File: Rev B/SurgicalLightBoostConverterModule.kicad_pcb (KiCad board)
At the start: 2 copper layers, 140 x 90 mm, 96 parts, among them J1 2x7 P2.54mm, Q1 BC337, Q10 BC327, Q2 BC337, Q3 BC337, Q4 AOT240L, Q5 AOT240L, Q6 AOT240L, Q7 BC327, Q8 BC327, Q9 BC327, U1 TL494, U2 TL431D, U3 LM358

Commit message: Silk screen.
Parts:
- moved J1 26.0 mm to (90.0, 103.7)
- moved TP11 12.2 mm to (90.0, 98.0)
- moved TP8 7.36 mm to (85.0, 98.0)
- moved TP9 7.32 mm to (79.5, 98.0)
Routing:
- net /1IN+: track 45.7 -> 37.0 mm
- net /DTC: track 33.6 -> 25.5 mm
- net /2IN+: track 42.8 -> 35.3 mm, vias 0 -> 1
- net Net-(JP6-A): track 39.0 -> 31.5 mm
- net Net-(JP2-A): track 47.0 -> 40.1 mm
- net /1IN-: track 40.8 -> 34.1 mm
- net Net-(JP3-A): track 35.5 -> 29.4 mm
- net /FB: track 37.3 -> 32.4 mm
- net /2IN-: track 36.1 -> 32.7 mm
- net +5V: track 66.1 -> 67.7 mm
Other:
- board text added: "24V 10A Fuse"

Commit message: Updated text for testpoints and jumpers.
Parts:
- renumbered TP9 to 1IN+, TP8 to 1IN-, TP11 to DTC
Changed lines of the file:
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@@
 		(descr "wire loop with bead as test point, loop diameter2.548mm, hole diameter 1.5mm")
 		(tags "test point wire loop bead")
-		(property "Reference" "TP8"
-			(at 0.7 2.5 0)
+		(property "Reference" "1IN-"
+			(at 0 3 0)
 			(layer "F.SilkS")
 			(effects
@@
 		)
 		(fp_text user "${REFERENCE}"
-			(at 0.7 2.5 0)
+			(at 0 3 0)
 			(layer "F.Fab")
 			(effects
@@
 		(descr "wire loop with bead as test point, loop diameter2.548mm, hole diameter 1.5mm")
 		(tags "test point wire loop bead")
-		(property "Reference" "TP9"
-			(at 0.7 2.5 0)
+		(property "Reference" "1IN+"
+			(at 0 3 0)
 			(layer "F.SilkS")
 			(effects
@@
 		)
 		(fp_text user "${REFERENCE}"
-			(at 0.7 2.5 0)
+			(at 0 3 0)
 			(layer "F.Fab")
 			(effects
@@
 		(descr "wire loop with bead as test point, loop diameter2.548mm, hole diameter 1.5mm")
 		(tags "test point wire loop bead")
-		(property "Reference" "TP11"
-			(at 0.7 2.5 0)
+		(property "Reference" "DTC"
+			(at 0 3 0)
 			(layer "F.SilkS")
 			(effects
@@
 		)
 		(fp_text user "${REFERENCE}"
-			(at 0.7 2.5 0)
-			(layer "F.Fab")
-			(effects
+			(at 0 3 0)
+			(layer "F.Fab")
+			(effects

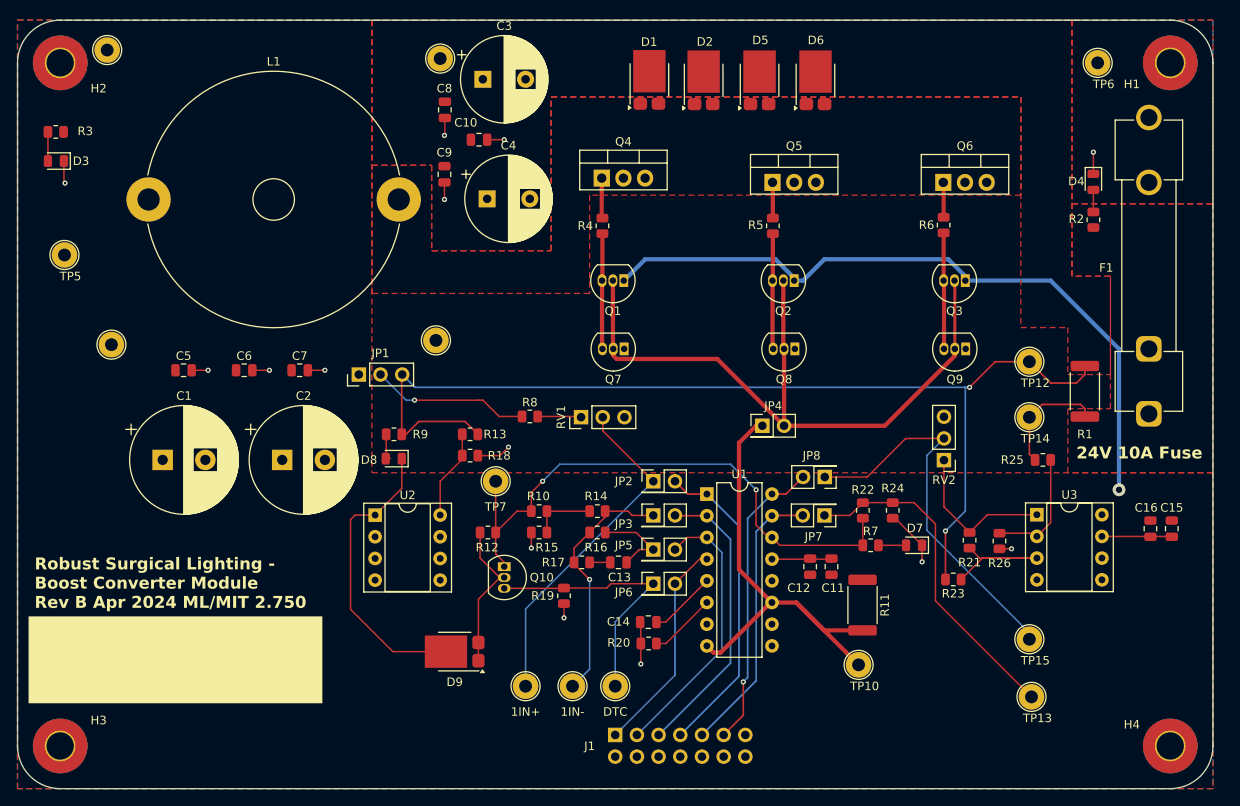
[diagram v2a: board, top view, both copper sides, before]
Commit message: Updated text for testpoints and jumpers.
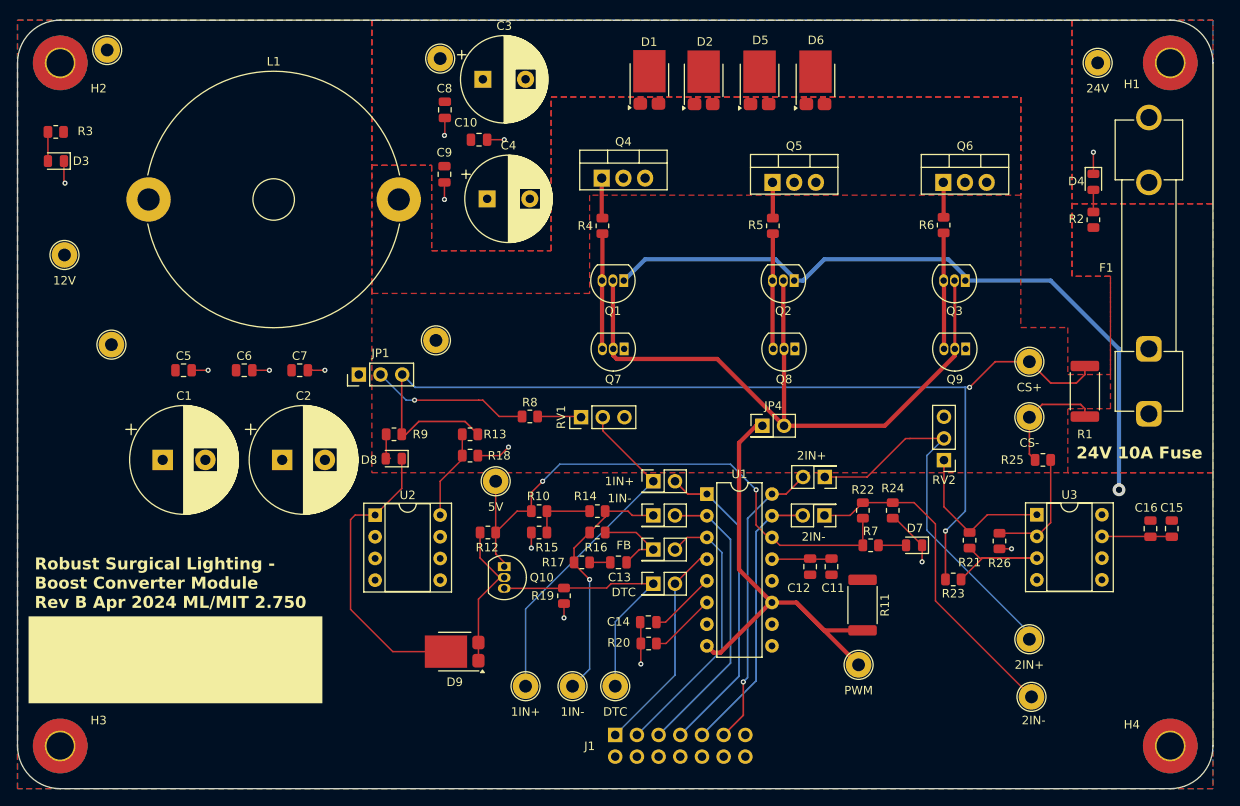
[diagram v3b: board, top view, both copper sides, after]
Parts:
- renumbered TP5 to 12V, JP2 to 1IN+, JP3 to 1IN-, TP6 to 24V, JP8 to 2IN+, TP15 to 2IN+, TP13 to 2IN-, JP7 to 2IN-, TP7 to 5V, TP12 to CS+, TP14 to CS-, JP6 to DTC, JP5 to FB, TP10 to PWM
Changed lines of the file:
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@@
 		(descr "wire loop with bead as test point, loop diameter2.548mm, hole diameter 1.5mm")
 		(tags "test point wire loop bead")
-		(property "Reference" "TP7"
+		(property "Reference" "5V"
 			(at 0 3 0)
 			(layer "F.SilkS")
@@
 		)
 		(fp_text user "${REFERENCE}"
-			(at 0.7 2.5 0)
+			(at 0 3 0)
 			(layer "F.Fab")
 			(effects
@@
 		(descr "wire loop with bead as test point, loop diameter2.548mm, hole diameter 1.5mm")
 		(tags "test point wire loop bead")
-		(property "Reference" "TP14"
-			(at 0.7 2.5 0)
+		(property "Reference" "CS-"
+			(at 0 3 0)
 			(layer "F.SilkS")
 			(effects
@@
 		)
 		(fp_text user "${REFERENCE}"
-			(at 0.7 2.5 0)
+			(at 0 3 0)
 			(layer "F.Fab")
 			(effects
@@
 		(descr "wire loop with bead as test point, loop diameter2.548mm, hole diameter 1.5mm")
 		(tags "test point wire loop bead")
-		(property "Reference" "TP13"
-			(at 0.7 2.5 0)
+		(property "Reference" "2IN-"
+			(at 0.25 2.75 0)
 			(layer "F.SilkS")
 			(effects
@@
 		)
 		(fp_text user "${REFERENCE}"
-			(at 0.7 2.5 0)
+			(at 0.25 2.75 0)
 			(layer "F.Fab")
 			(effects
@@
 		(tags "resistor")
 		(property "Reference" "R14"
-			(at -0.1625 -1.75 0)
+			(at -1.4125 -1.75 0)
 			(layer "F.SilkS")
 			(effects
@@
 		)
 		(property "Value" "1K"
-			(at 0 -2 0)
+			(at -0.4125 -2.5 0)
 			(layer "F.Fab")
 			(effects
@@
 		(descr "Through hole straight pin header, 2x01, 2.54mm pitch, double rows")
 		(tags "Through hole pin header THT 2x01 2.54mm double row")
-		(property "Reference" "JP6"
+		(property "Reference" "DTC"
 			(at -3.46 1 0)
 			(layer "F.SilkS")
@@
 		(descr "Through hole straight pin header, 2x01, 2.54mm pitch, double rows")
 		(tags "Through hole pin header THT 2x01 2.54mm double row")
-		(property "Reference" "JP7"
+		(property "Reference" "2IN-"
 			(at 1.27 -2.5 180)
 			(layer "F.SilkS")
@@
 		(descr "Through hole straight pin header, 2x01, 2.54mm pitch, double rows")
 		(tags "Through hole pin header THT 2x01 2.54mm double row")
-		(property "Reference" "JP3"
-			(at -3.46 1 0)
+		(property "Reference" "1IN-"
+			(at -3.96 -2 0)
 			(layer "F.SilkS")
 			(effects
@@
 		(descr "Through hole straight pin header, 2x01, 2.54mm pitch, double rows")
 		(tags "Through hole pin header THT 2x01 2.54mm double row")
-		(property "Reference" "JP8"
+		(property "Reference" "2IN+"
 			(at 1.54 2.5 180)
 			(layer "F.SilkS")
@@
 		(descr "Through hole straight pin header, 2x01, 2.54mm pitch, double rows")
 		(tags "Through hole pin header THT 2x01 2.54mm double row")
-		(property "Reference" "JP5"
+		(property "Reference" "FB"
 			(at -3.46 -0.5 0)
 			(layer "F.SilkS")
@@
 		(descr "wire loop with bead as test point, loop diameter2.548mm, hole diameter 1.5mm")
 		(tags "test point wire loop bead")
-		(property "Reference" "TP5"
-			(at 0.7 2.5 0)
+		(property "Reference" "12V"
+			(at 0 3 0)
 			(layer "F.SilkS")
 			(effects
@@
 		)
 		(fp_text user "${REFERENCE}"
-			(at 0.7 2.5 0)
+			(at 0 3 0)
 			(layer "F.Fab")
 			(effects
@@
 		(descr "Through hole straight pin header, 2x01, 2.54mm pitch, double rows")
 		(tags "Through hole pin header THT 2x01 2.54mm double row")
-		(property "Reference" "JP2"
-			(at -3.46 0 0)
+		(property "Reference" "1IN+"
+			(at -3.96 0 0)
 			(layer "F.SilkS")
 			(effects
@@
 		(descr "wire loop with bead as test point, loop diameter2.548mm, hole diameter 1.5mm")
 		(tags "test point wire loop bead")
-		(property "Reference" "TP12"
-			(at 0.7 2.5 0)
+		(property "Reference" "CS+"
+			(at 0 3 0)
 			(layer "F.SilkS")
 			(effects
@@
 		)
 		(fp_text user "${REFERENCE}"
-			(at 0.7 2.5 0)
+			(at 0 3 0)
 			(layer "F.Fab")
 			(effects
@@
 		(descr "wire loop with bead as test point, loop diameter2.548mm, hole diameter 1.5mm")
 		(tags "test point wire loop bead")
-		(property "Reference" "TP6"
-			(at 0.7 2.5 0)
+		(property "Reference" "24V"
+			(at 0 3 0)
 			(layer "F.SilkS")
 			(effects
@@
 		)
 		(fp_text user "${REFERENCE}"
-			(at 0.7 2.5 0)
+			(at 0 3 0)
 			(layer "F.Fab")
 			(effects
@@
 		(descr "wire loop with bead as test point, loop diameter2.548mm, hole diameter 1.5mm")
 		(tags "test point wire loop bead")
-		(property "Reference" "TP10"
-			(at 0.7 2.5 0)
+		(property "Reference" "PWM"
+			(at 0 3 0)
 			(layer "F.SilkS")
 			(effects
@@
 		)
 		(fp_text user "${REFERENCE}"
-			(at 0.7 2.5 0)
+			(at 0 3 0)
 			(layer "F.Fab")
 			(effects
@@
 		(descr "wire loop with bead as test point, loop diameter2.548mm, hole diameter 1.5mm")
 		(tags "test point wire loop bead")
-		(property "Reference" "TP15"
-			(at 0.7 2.5 0)
+		(property "Reference" "2IN+"
+			(at 0 3 0)
 			(layer "F.SilkS")
 			(effects
@@
 		)
 		(fp_text user "${REFERENCE}"
-			(at 0.7 2.5 0)
+			(at 0 3 0)
 			(layer "F.Fab")
 			(effects
